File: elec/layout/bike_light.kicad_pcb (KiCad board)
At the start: 2 copper layers, 40 x 40 mm, 21 parts

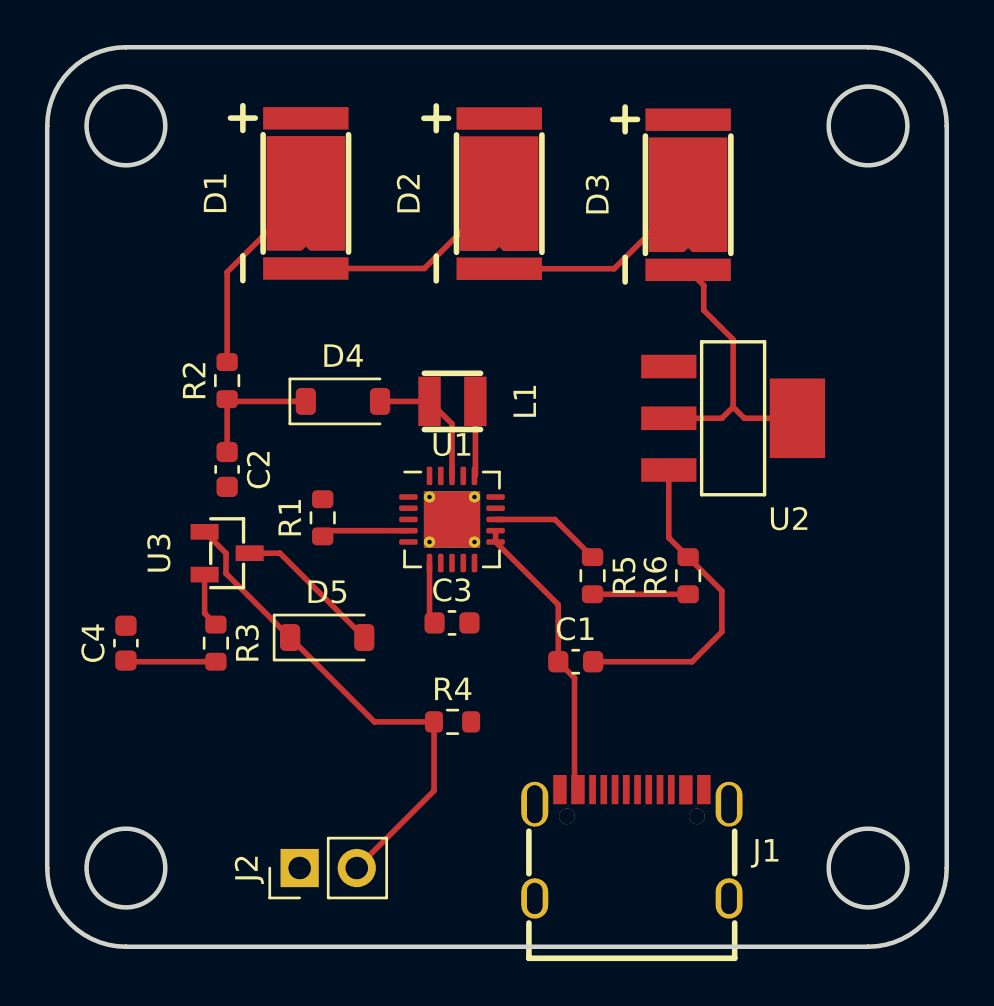
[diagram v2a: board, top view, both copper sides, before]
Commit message: start routing traces
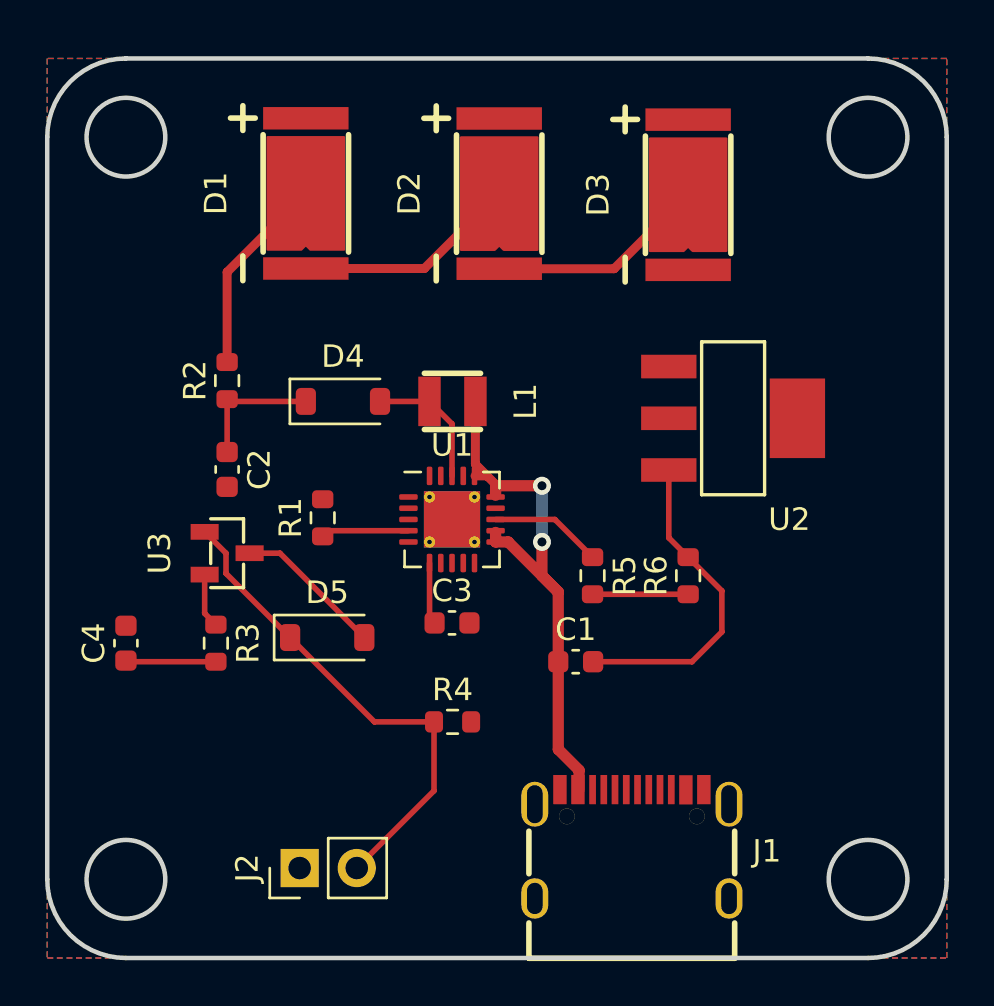
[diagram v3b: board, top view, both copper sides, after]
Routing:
- net 9: track 13.1 -> 0.00 mm
- net 1: track 16.3 -> 25.5 mm, vias 0 -> 2
- added copper zone on B.Cu, net 2
- added copper zone on F.Cu, net 2
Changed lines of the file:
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@@
   )
   (setup
+    (stackup
+      (layer "F.SilkS" (type "Top Silk Screen"))
+      (layer "F.Paste" (type "Top Solder Paste"))
+      (layer "F.Mask" (type "Top Solder Mask") (thickness 0.01))
+      (layer "F.Cu" (type "copper") (thickness 0.035))
+      (layer "dielectric 1" (type "core") (thickness 1.51) (material "FR4") (epsilon_r 4.5) (loss_tangent 0.02))
+      (layer "B.Cu" (type "copper") (thickness 0.035))
+      (layer "B.Mask" (type "Bottom Solder Mask") (thickness 0.01))
+      (layer "B.Paste" (type "Bottom Solder Paste"))
+      (layer "B.SilkS" (type "Bottom Silk Screen"))
+      (copper_finish "None")
+      (dielectric_constraints no)
+    )
     (pad_to_mask_clearance 0)
     (grid_origin 100 100)
@@
     )
   )
-  (gr_circle (center 136.5 103) (end 138.25 103)
+  (gr_circle (center 136.5 103.5) (end 138.25 103.5)
     (stroke (width 0.2) (type solid)) (fill none) (layer "Edge.Cuts"))
-  (gr_circle (center 103.5 103) (end 105.25 103)
+  (gr_circle (center 103.5 103.5) (end 105.25 103.5)
     (stroke (width 0.2) (type solid)) (fill none) (layer "Edge.Cuts"))
-  (gr_arc (start 140 136) (mid 138.974874 138.474874) (end 136.5 139.5)
+  (gr_arc (start 140 136.5) (mid 138.974874 138.974874) (end 136.5 140)
     (stroke (width 0.2) (type solid)) (layer "Edge.Cuts"))
-  (gr_arc (start 136.5 99.5) (mid 138.974874 100.525126) (end 140 103)
+  (gr_arc (start 136.5 100) (mid 138.974874 101.025126) (end 140 103.5)
     (stroke (width 0.2) (type solid)) (layer "Edge.Cuts"))
-  (gr_line (start 140 136) (end 140 103)
+  (gr_line (start 140 136.5) (end 140 103.5)
     (stroke (width 0.2) (type solid)) (layer "Edge.Cuts"))
-  (gr_line (start 103.5 139.5) (end 136.5 139.5)
+  (gr_line (start 103.5 140) (end 136.5 140)
     (stroke (width 0.2) (type solid)) (layer "Edge.Cuts"))
-  (gr_arc (start 103.5 139.5) (mid 101.025126 138.474874) (end 100 136)
+  (gr_arc (start 103.5 140) (mid 101.025126 138.974874) (end 100 136.5)
     (stroke (width 0.2) (type solid)) (layer "Edge.Cuts"))
-  (gr_circle (center 103.5 136) (end 105.25 136)
+  (gr_circle (center 103.5 136.5) (end 105.25 136.5)
     (stroke (width 0.2) (type solid)) (fill none) (layer "Edge.Cuts"))
-  (gr_circle (center 136.5 136) (end 138.25 136)
+  (gr_circle (center 136.5 136.5) (end 138.25 136.5)
     (stroke (width 0.2) (type solid)) (fill none) (layer "Edge.Cuts"))
-  (gr_line (start 100 136) (end 100 103)
+  (gr_line (start 100 136.5) (end 100 103.5)
     (stroke (width 0.2) (type solid)) (layer "Edge.Cuts"))
-  (gr_arc (start 100 103) (mid 101.025126 100.525126) (end 103.5 99.5)
+  (gr_arc (start 100 103.5) (mid 101.025126 101.025126) (end 103.5 100)
     (stroke (width 0.2) (type solid)) (layer "Edge.Cuts"))
-  (gr_line (start 103.5 99.5) (end 136.5 99.5)
+  (gr_line (start 103.5 100) (end 136.5 100)
     (stroke (width 0.2) (type solid)) (layer "Edge.Cuts"))
   (segment (start 110.8 125.75) (end 107.95 122.9) (width 0.25) (layer "F.Cu") (net 1))
@@
   (segment (start 130 125.5) (end 130 123.675) (width 0.25) (layer "F.Cu") (net 2))
   (segment (start 128.5 122.175) (end 127.64 121.315) (width 0.25) (layer "F.Cu") (net 2))
-  (segment (start 108 109.5) (end 111.5 106) (width 0.25) (layer "F.Cu") (net 3))
-  (segment (start 108 113.5) (end 108 109.5) (width 0.25) (layer "F.Cu") (net 3))
-  (segment (start 119 118.5625) (end 119.04 118.5225) (width 0.25) (layer "F.Cu") (net 4))
-  (segment (start 123.45 127.55) (end 122.725 126.825) (width 0.25) (layer "F.Cu") (net 4))
-  (segment (start 122.725 124.2875) (end 119.9375 121.5) (width 0.25) (layer "F.Cu") (net 4))
-  (segment (start 119.04 118.5225) (end 119.04 115.25) (width 0.25) (layer "F.Cu") (net 4))
-  (segment (start 119.9375 121.5) (end 119.9375 121) (width 0.25) (layer "F.Cu") (net 4))
-  (segment (start 123.45 132.5125) (end 123.45 127.55) (width 0.25) (layer "F.Cu") (net 4))
-  (segment (start 122.725 126.825) (end 122.725 124.2875) (width 0.25) (layer "F.Cu") (net 4))
+  (segment (start 108 113.5) (end 108 109.5) (width 0.4) (layer "F.Cu") (net 3))
+  (segment (start 108 109.5) (end 111.5 106) (width 0.4) (layer "F.Cu") (net 3))
+  (segment (start 120 119) (end 119.5625 118.5625) (width 0.4) (layer "F.Cu") (net 4))
+  (segment (start 122.725 130.725) (end 123.65 131.65) (width 0.5) (layer "F.Cu") (net 4))
+  (segment (start 122.725 126.825) (end 122.725 123.725) (width 0.5) (layer "F.Cu") (net 4))
+  (segment (start 119.9375 121.5) (end 119.9375 121.075) (width 0.5) (layer "F.Cu") (net 4))
+  (segment (start 122 119) (end 120 119) (width 0.5) (layer "F.Cu") (net 4))
+  (segment (start 119.04 118.04) (end 119.5625 118.5625) (width 0.4) (layer "F.Cu") (net 4))
+  (segment (start 119.04 115.25) (end 119.04 118.04) (width 0.4) (layer "F.Cu") (net 4))
+  (segment (start 119.9375 119.0625) (end 119.9375 119.425) (width 0.5) (layer "F.Cu") (net 4))
+  (segment (start 120.5 121.5) (end 119.9375 121.5) (width 0.5) (layer "F.Cu") (net 4))
+  (segment (start 122.725 123.725) (end 122 123) (width 0.5) (layer "F.Cu") (net 4))
+  (segment (start 123.65 131.65) (end 123.65 132.5125) (width 0.5) (layer "F.Cu") (net 4))
+  (segment (start 119.5625 118.5625) (end 119.025 118.5625) (width 0.4) (layer "F.Cu") (net 4))
+  (segment (start 122.725 126.825) (end 122.725 130.725) (width 0.5) (layer "F.Cu") (net 4))
+  (segment (start 122.725 123.725) (end 120.5 121.5) (width 0.5) (layer "F.Cu") (net 4))
+  (segment (start 120 119) (end 119.9375 119.0625) (width 0.5) (layer "F.Cu") (net 4))
+  (segment (start 122 123) (end 122 121.5) (width 0.5) (layer "F.Cu") (net 4))
+  (via (at 122 119) (size 0.8) (drill 0.4) (layers "F.Cu" "B.Cu") (net 4))
+  (via (at 122 121.5) (size 0.8) (drill 0.4) (layers "F.Cu" "B.Cu") (net 4))
+  (segment (start 122 121.5) (end 122 119) (width 0.5) (layer "B.Cu") (net 4))
   (segment (start 117.225 125.1) (end 117 124.875) (width 0.25) (layer "F.Cu") (net 6))
   (segment (start 117 124.875) (end 117 122.4375) (width 0.25) (layer "F.Cu") (net 6))
-  (segment (start 120.1 109.35) (end 125.21 109.35) (width 0.25) (layer "F.Cu") (net 7))
-  (segment (start 125.21 109.35) (end 128.5 106.06) (width 0.25) (layer "F.Cu") (net 7))
+  (segment (start 125.21 109.35) (end 128.5 106.06) (width 0.4) (layer "F.Cu") (net 7))
+  (segment (start 120.1 109.35) (end 125.21 109.35) (width 0.4) (layer "F.Cu") (net 7))
   (segment (start 112.5 121) (end 112.25 121.25) (width 0.25) (layer "F.Cu") (net 9))
   (segment (start 116.0625 121) (end 112.5 121) (width 0.25) (layer "F.Cu") (net 9))
@@
   (segment (start 110.35 122) (end 114.1 125.75) (width 0.25) (layer "F.Cu") (net 12))
   (segment (start 109 122) (end 110.35 122) (width 0.25) (layer "F.Cu") (net 12))
-  (segment (start 129.195 111.195) (end 130.5 112.5) (width 0.25) (layer "F.Cu") (net 13))
-  (segment (start 130.5 115.5) (end 130 116) (width 0.25) (layer "F.Cu") (net 13))
-  (segment (start 129.195 110.095) (end 129.195 111.195) (width 0.25) (layer "F.Cu") (net 13))
-  (segment (start 130 116) (end 127.64 116) (width 0.25) (layer "F.Cu") (net 13))
-  (segment (start 130.5 112.5) (end 130.5 115.5) (width 0.25) (layer "F.Cu") (net 13))
-  (segment (start 133.36 116) (end 131 116) (width 0.25) (layer "F.Cu") (net 13))
-  (segment (start 128.5 109.4) (end 129.195 110.095) (width 0.25) (layer "F.Cu") (net 13))
-  (segment (start 131 116) (end 130.5 115.5) (width 0.25) (layer "F.Cu") (net 13))
-  (segment (start 116.77 109.34) (end 120.1 106.01) (width 0.25) (layer "F.Cu") (net 14))
-  (segment (start 111.5 109.34) (end 116.77 109.34) (width 0.25) (layer "F.Cu") (net 14))
+  (segment (start 111.5 109.34) (end 116.77 109.34) (width 0.4) (layer "F.Cu") (net 14))
+  (segment (start 116.77 109.34) (end 120.1 106.01) (width 0.4) (layer "F.Cu") (net 14))
   (segment (start 108.1 115.25) (end 108 115.15) (width 0.25) (layer "F.Cu") (net 15))
   (segment (start 108 115.15) (end 108 117.5) (width 0.25) (layer "F.Cu") (net 15))
@@
   (segment (start 103.55 126.825) (end 103.5 126.775) (width 0.25) (layer "F.Cu") (net 18))
   (segment (start 124.25 123.825) (end 128.5 123.825) (width 0.25) (layer "F.Cu") (net 19))
+  (zone (net 2) (net_name "2") (layers "F&B.Cu") (hatch edge 0.5)
+    (connect_pads (clearance 0.5))
+    (min_thickness 0.25) (filled_areas_thickness no)
+    (fill yes (thermal_gap 0.5) (thermal_bridge_width 0.5))
+    (polygon
+      (pts
+        (xy 100 100)
+        (xy 100 140)
+        (xy 140 140)
+        (xy 140 100)
+      )
+    )
+  )
   (group "" (id ba4d4596-1074-4429-bbeb-256b845808bd)
     (members

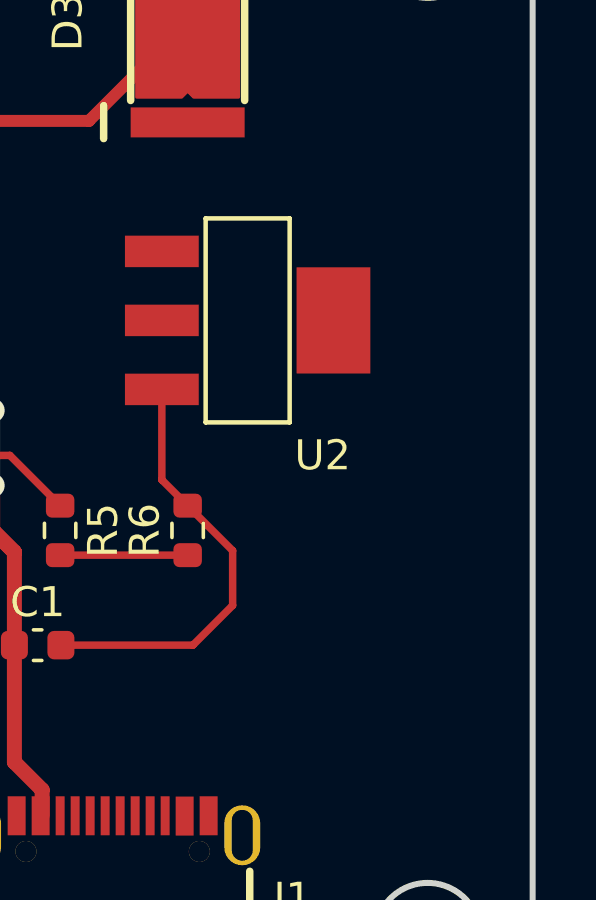
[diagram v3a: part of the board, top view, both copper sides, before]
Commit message: add githash label to PCB
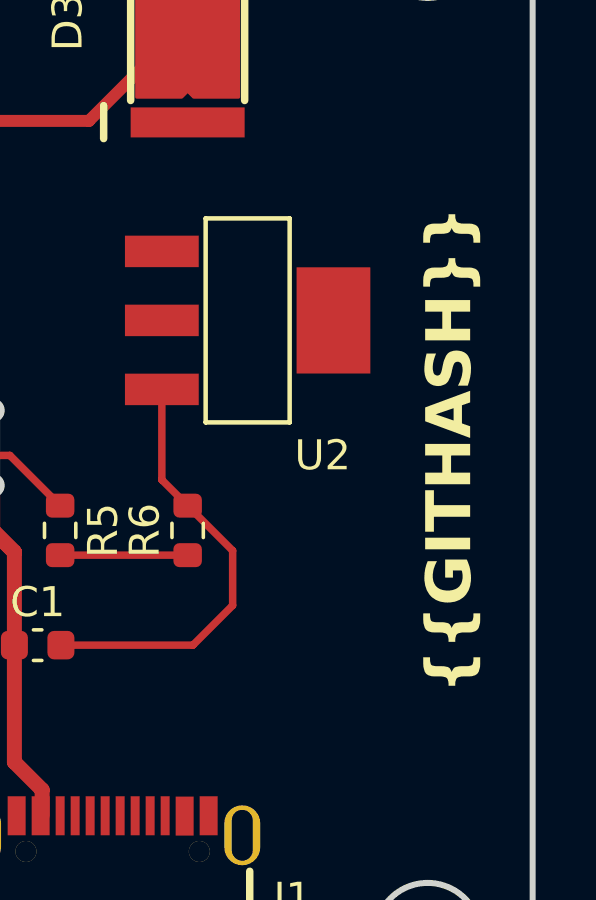
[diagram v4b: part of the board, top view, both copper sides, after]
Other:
- board text added: "{{GITHASH}}"
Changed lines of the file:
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@@
   (gr_line (start 103.5 100) (end 136.5 100)
     (stroke (width 0.2) (type solid)) (layer "Edge.Cuts"))
+  (gr_text "{{GITHASH}}" (at 138.1 120.32 90) (layer "F.SilkS")
+    (effects (font (size 1.5 1.5) (thickness 0.3) bold) (justify bottom))
+  )
   (segment (start 110.8 125.75) (end 107.95 122.9) (width 0.25) (layer "F.Cu") (net 1))
   (segment (start 117.2 132.565) (end 117.2 129.5) (width 0.25) (layer "F.Cu") (net 1))

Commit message: finish layout
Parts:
- moved C3 0.91 mm to (117.1, 125.4), turned to -90 degrees
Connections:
- D1 pad 2: 5 -> (no net)
- D1 pad 3: (no net) -> 5
- D2 pad 2: 4 -> (no net)
- D2 pad 3: (no net) -> 4
- D3 pad 2: 7 -> (no net)
- D3 pad 3: (no net) -> 7
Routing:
- net 12: track 22.2 -> 60.7 mm
- net 5: track 8.95 -> 39.2 mm
- net 11: track 10.9 -> 29.5 mm, vias 0 -> 2
- net 9: track 0.00 -> 18.6 mm
- net 1: track 25.5 -> 42.6 mm, vias 2 -> 4
- net 2: track 14.5 -> 25.5 mm
- net 17: track 4.25 -> 14.6 mm, vias 0 -> 2
- net 16: track 6.65 -> 14.0 mm
- net 7: track 9.76 -> 13.4 mm
- net 4: track 9.98 -> 13.0 mm
- net 15: track 2.76 -> 2.25 mm
- net 18: track 0.00 -> 0.50 mm
